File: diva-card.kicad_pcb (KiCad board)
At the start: 2 copper layers, 85.4 x 53.7 mm, 94 parts, among them J1 Conn_02x05_Odd_Even, J2 USB_C_Receptacle_USB2.0, J3 Conn_02x21_Odd_Even, SW1 USER, SW2 BOOTSEL, SW3 RESET, U1 AP2112K-3.3, U2 ATECC608A-MAHDA, U3 W25Q128XXX, U4 RP2040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

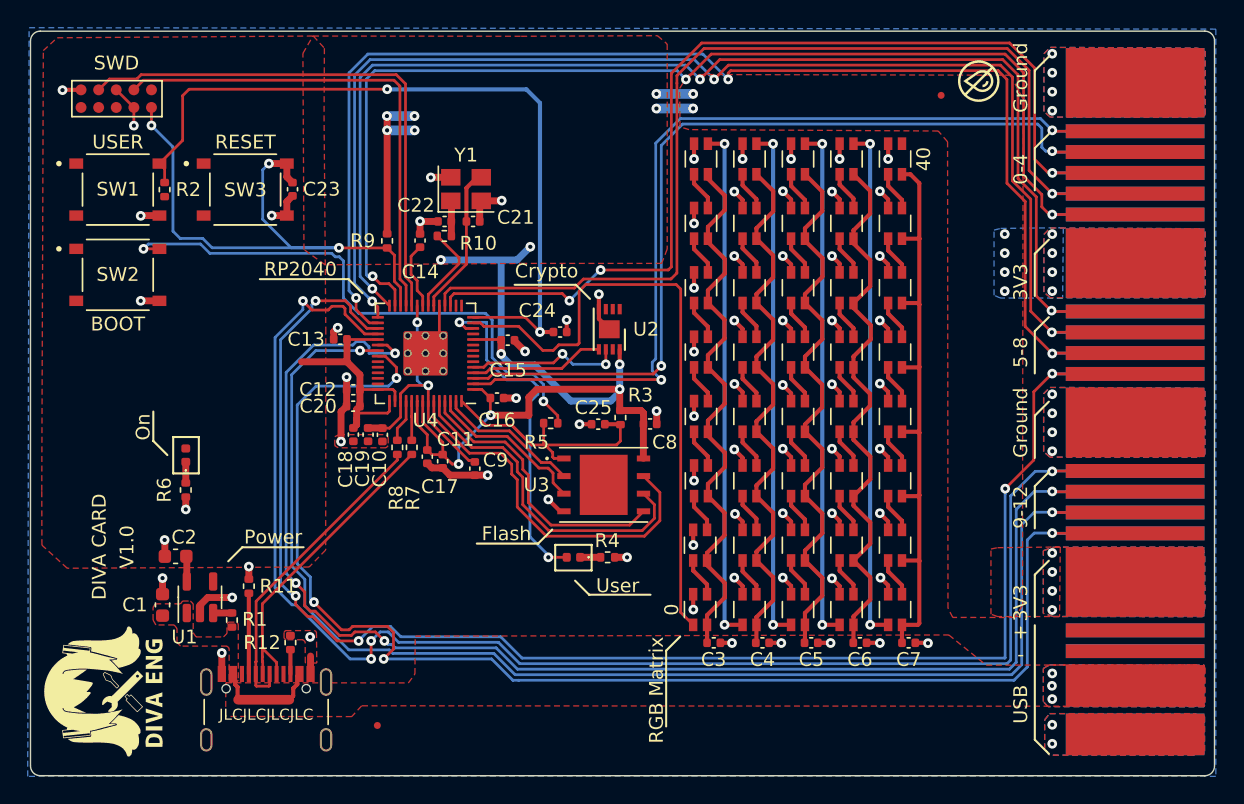
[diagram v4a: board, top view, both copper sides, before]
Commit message: Remove trace under usb trace
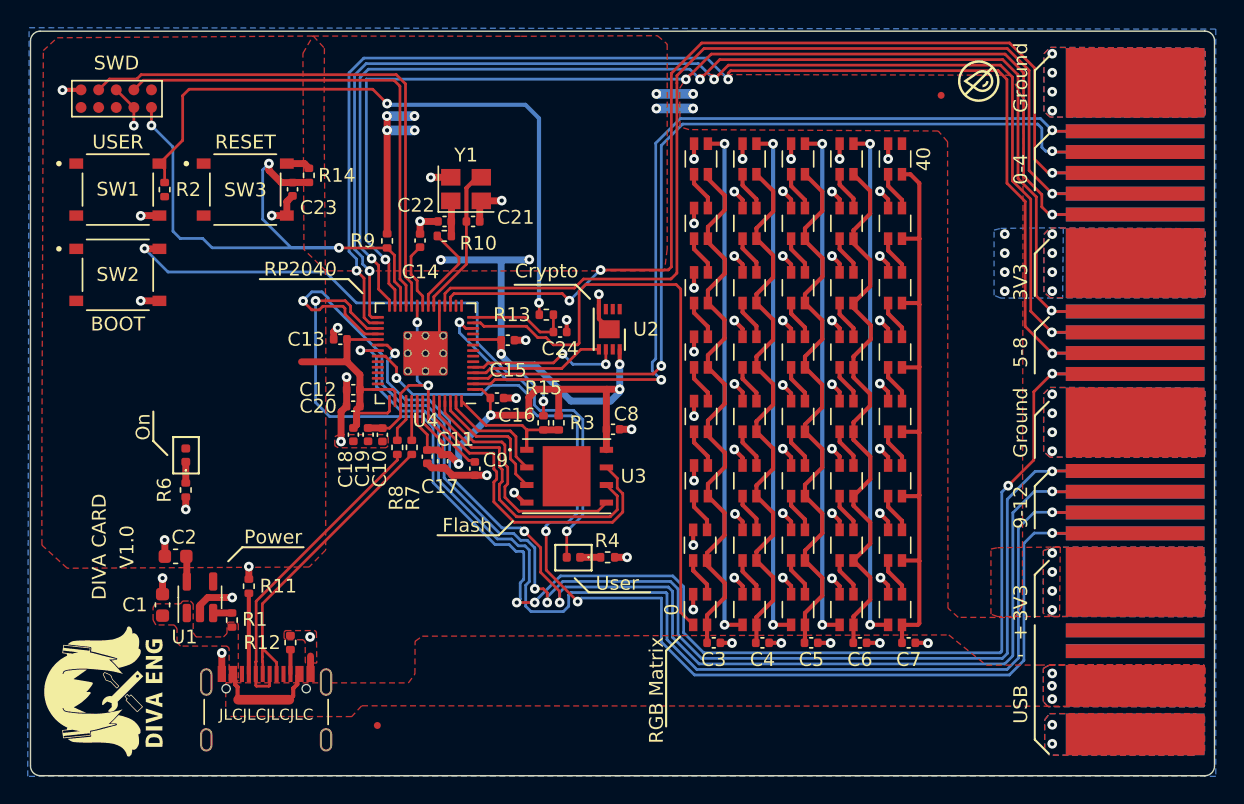
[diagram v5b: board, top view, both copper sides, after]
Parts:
- removed C25: 1u, Capacitor_SMD:C_0402_1005Metric
- removed R5: 1k, Resistor_SMD:R_0402_1005Metric
- added R13: 10k, Resistor_SMD:R_0402_1005Metric, F.Cu at (100.8, 81.1)
- added R14: 10k, Resistor_SMD:R_0402_1005Metric, F.Cu at (83.7, 71.0)
- added R15: 1K, Resistor_SMD:R_0402_1005Metric, F.Cu at (100.6, 88.9)
- R10: value DNF -> 100
- R2: value 5k -> 10k
- moved R3 4.47 mm to (101.7, 88.9)
- moved U3 2.75 mm to (102.3, 92.8)
- moved C8 2.70 mm to (105.6, 89.4)
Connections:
- R2 pad 2: /~{USER_SW0} -> Net-(R2-Pad2)
- SW1 pad 1: /~{USER_SW0} -> Net-(R2-Pad2)
- SW2 pad 1: /peripherals/~{USB_BOOT} -> /peripherals/~{BOOT_SEL}
- SW3 pad 1: /connectors/~{RESET} -> Net-(R14-Pad2)
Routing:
- net /~{USER_SW0}: track 56.2 -> 7.48 mm, vias 2 -> 0
- net Net-(R2-Pad2): track 0.00 -> 48.1 mm, vias 0 -> 2
- net /peripherals/~{USB_BOOT}: track 40.7 -> 0.00 mm, vias 2 -> 0
- net /peripherals/~{BOOT_SEL}: track 0.00 -> 37.4 mm, vias 0 -> 2
- net /connectors/USER_IO_10: track 108.0 -> 90.5 mm
- net /connectors/USER_IO_12: track 104.8 -> 93.1 mm
- net /connectors/USER_IO_11: track 102.7 -> 92.7 mm
- net /microcontroller/~{QSPI_CS}: track 20.7 -> 10.7 mm
- net /connectors/USER_IO_9: track 113.8 -> 105.5 mm
- net /connectors/USER_IO_8: track 116.6 -> 112.2 mm
- net /microcontroller/QSPI_SIO3: track 26.8 -> 24.2 mm
- net /microcontroller/QSPI_SCLK: track 24.0 -> 21.6 mm
- net /microcontroller/QSPI_SIO0: track 20.5 -> 18.1 mm
- net /microcontroller/QSPI_SIO2: track 11.8 -> 9.68 mm
- net /microcontroller/QSPI_SIO1: track 10.3 -> 8.25 mm
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
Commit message: update power delivery
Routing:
- net +3V3: track 108.0 -> 57.7 mm, vias 27 -> 19
- net /connectors/~{RESET}: track 44.5 -> 41.9 mm
- net /microcontroller/XOUT: track 6.60 -> 5.30 mm
- net GND: track 105.6 -> 104.3 mm
- net /connectors/USER_IO_4: track 89.1 -> 89.9 mm
- net /connectors/USER_IO_3: track 80.9 -> 81.6 mm, vias 1 -> 3
